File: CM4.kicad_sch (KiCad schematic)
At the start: 2 parts

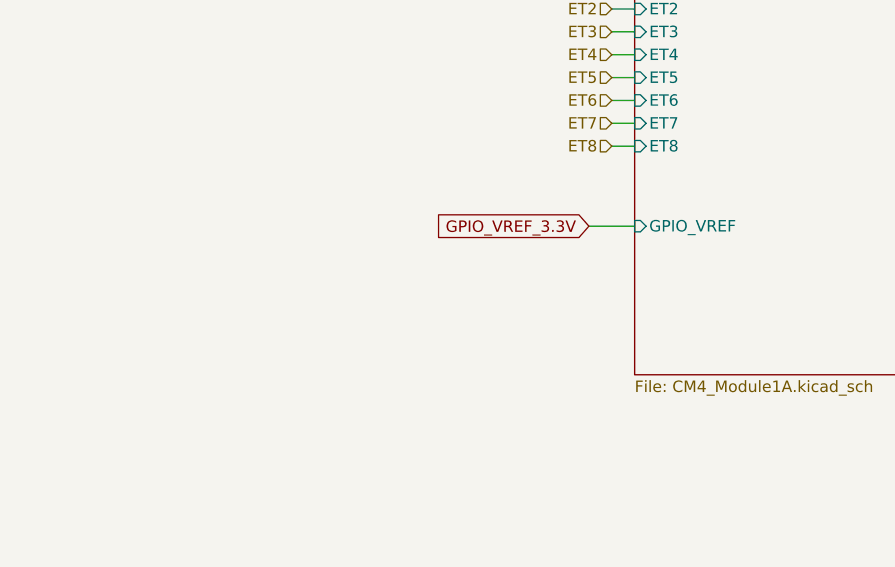
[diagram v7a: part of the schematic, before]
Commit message: checked the whole schematic with the datasheet, took notes/questions in the datasheet (pdf also uploaded)
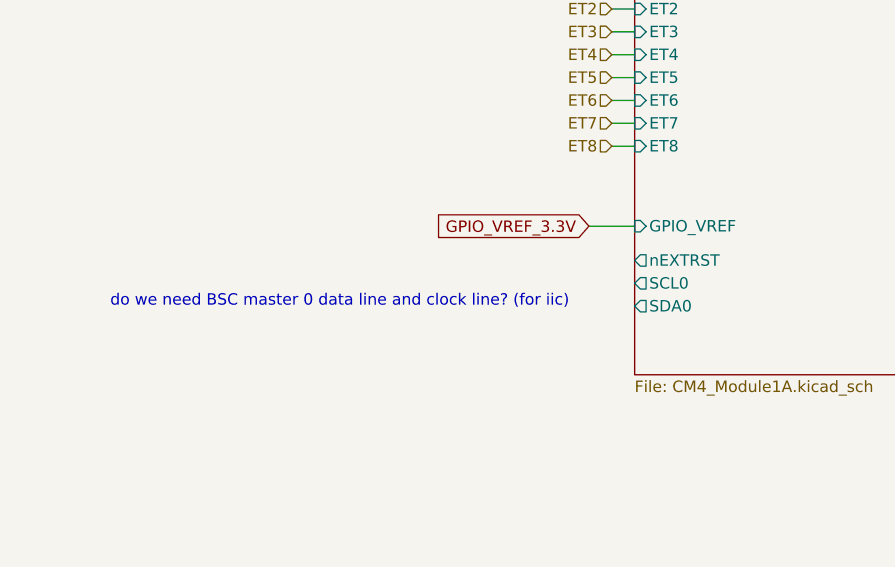
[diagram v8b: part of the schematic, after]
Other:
- sheet CM4_Module1A ports: added SCL0, SDA0, nEXTRST; removed none
- note added: "do we need BSC master 0 data line and clock line? (for iic)"
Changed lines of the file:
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@@
+		)
+	)
+	(text "do we need BSC master 0 data line and clock line? (for iic)"
+		(exclude_from_sim no)
+		(at 53.594 89.662 0)
+		(effects
+			(font
+				(size 1.27 1.27)
+			)
 		)
 	)
@@
 			(effects
 				(font
+					(size 1.27 1.27)
+				)
+				(justify left)
+			)
+		)
+		(pin "nEXTRST" output
+			(at 86.36 85.09 180)
+			(effects
+				(font
+					(size 1.27 1.27)
+				)
+				(justify left)
+			)
+		)
+		(pin "SCL0" output
+			(at 86.36 87.63 180)
+			(effects
+				(font
+					(size 1.27 1.27)
+				)
+				(justify left)
+			)
+		)
+		(pin "SDA0" output
+			(at 86.36 90.17 180)
+			(effects
+				(font
